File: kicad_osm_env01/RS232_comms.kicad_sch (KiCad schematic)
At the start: 17 parts

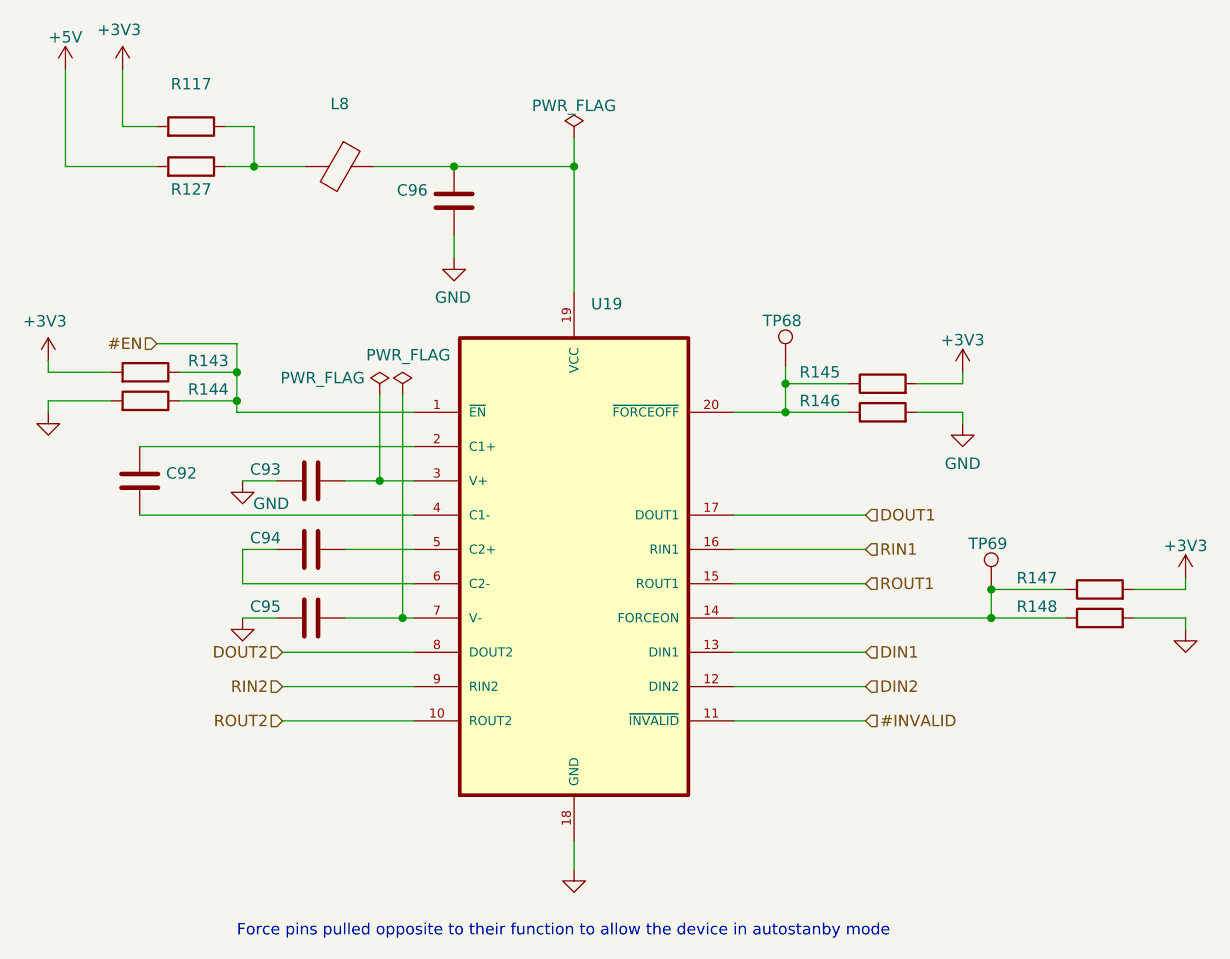
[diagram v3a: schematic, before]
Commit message: majority of signals routed on layout
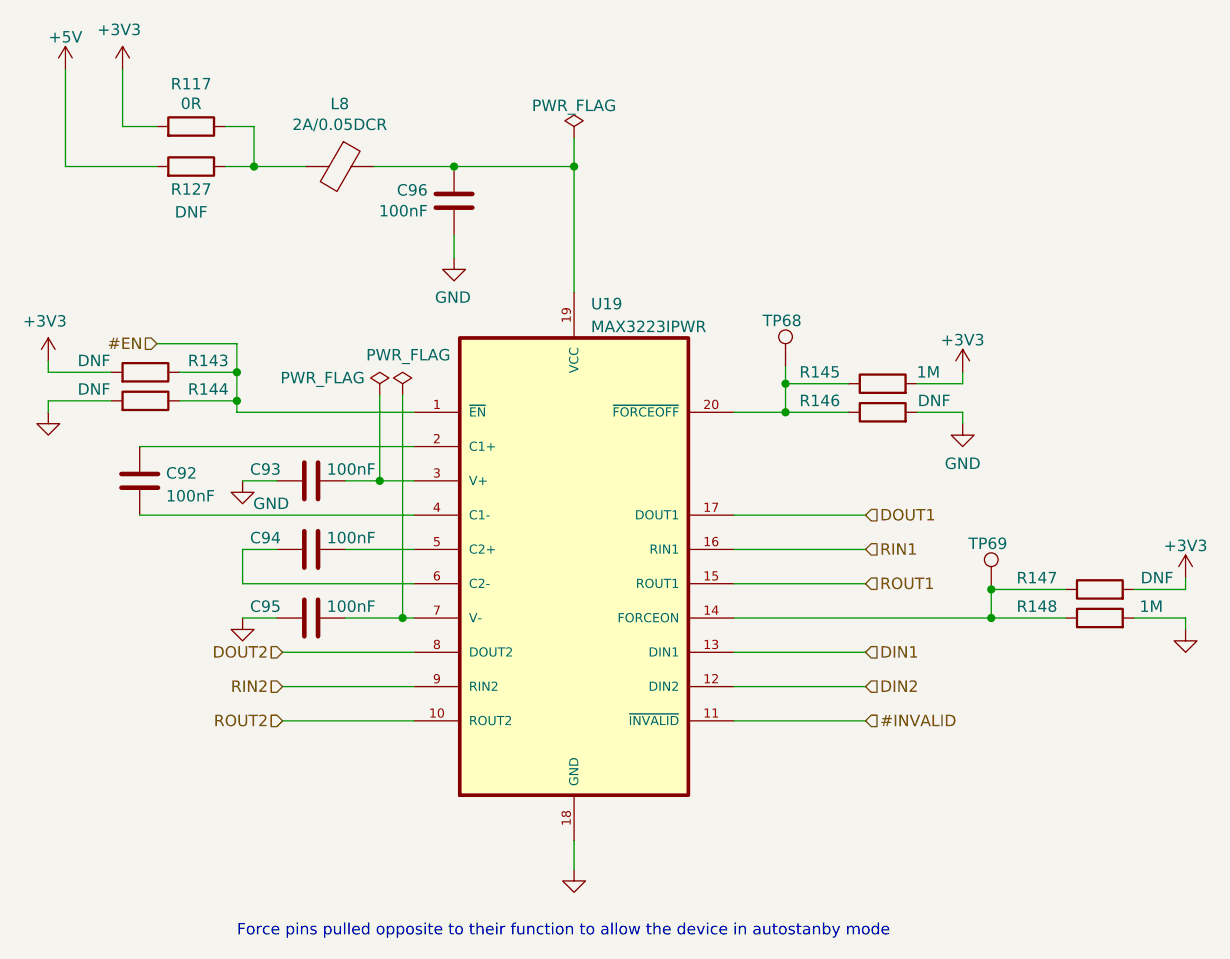
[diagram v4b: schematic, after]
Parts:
- C92, C93, C94, C95, C96: value (none) -> 100nF; footprint (none) -> Capacitor_SMD:C_0402_1005Metric
- L8: value (none) -> 2A/0.05DCR; footprint (none) -> Inductor_SMD:L_0402_1005Metric
- R117: value (none) -> 0R; footprint (none) -> Resistor_SMD:R_0603_1608Metric
- R127, R143, R144, R146, R147: value (none) -> DNF; footprint (none) -> Resistor_SMD:R_0603_1608Metric
- R145, R148: value (none) -> 1M; footprint (none) -> Resistor_SMD:R_0603_1608Metric
- TP68, TP69: value (none) -> Test_Point; footprint (none) -> TestPoint:TestPoint_THTPad_D1.0mm_Drill0.5mm
- U19: value (none) -> MAX3223IPWR; footprint (none) -> Package_SO:TSSOP-20_4.4x6.5mm_P0.65mm
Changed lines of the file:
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@@
     (in_bom yes) (on_board yes)
     (property "Reference" "L8" (id 0) (at 123.19 49.5554 90))
-    (property "Value" "" (id 1) (at 123.19 51.8668 90))
-    (property "Footprint" "" (id 2) (at 123.19 54.737 90)
+    (property "Value" "2A/0.05DCR" (id 1) (at 123.19 51.8668 90))
+    (property "Footprint" "Inductor_SMD:L_0402_1005Metric" (id 2) (at 123.19 54.737 90)
       (effects (font (size 1.27 1.27)) hide)
     )
@@
     (in_bom yes) (on_board yes)
     (property "Reference" "R117" (id 0) (at 106.68 47.3542 90))
-    (property "Value" "" (id 1) (at 106.68 49.53 90))
-    (property "Footprint" "" (id 2) (at 106.68 53.848 90)
+    (property "Value" "0R" (id 1) (at 106.68 49.53 90))
+    (property "Footprint" "Resistor_SMD:R_0603_1608Metric" (id 2) (at 106.68 53.848 90)
       (effects (font (size 1.27 1.27)) hide)
     )
@@
       (effects (font (size 1.27 1.27)) (justify left))
     )
-    (property "Value" "" (id 1) (at 132.969 61.468 0)
-      (effects (font (size 1.27 1.27)) (justify left))
-    )
-    (property "Footprint" "" (id 2) (at 134.9248 64.135 0)
+    (property "Value" "100nF" (id 1) (at 132.969 61.468 0)
+      (effects (font (size 1.27 1.27)) (justify left))
+    )
+    (property "Footprint" "Capacitor_SMD:C_0402_1005Metric" (id 2) (at 134.9248 64.135 0)
       (effects (font (size 1.27 1.27)) hide)
     )
@@
       (effects (font (size 1.27 1.27)) (justify left))
     )
-    (property "Value" "" (id 1) (at 151.1047 74.3259 0)
-      (effects (font (size 1.27 1.27)) (justify left))
-    )
-    (property "Footprint" "" (id 2) (at 149.225 100.965 0)
+    (property "Value" "MAX3223IPWR" (id 1) (at 151.1047 74.3259 0)
+      (effects (font (size 1.27 1.27)) (justify left))
+    )
+    (property "Footprint" "Package_SO:TSSOP-20_4.4x6.5mm_P0.65mm" (id 2) (at 149.225 100.965 0)
       (effects (font (size 1.27 1.27)) (justify left bottom) hide)
     )
@@
     (in_bom yes) (on_board yes)
     (property "Reference" "R144" (id 0) (at 108.585 81.28 90))
-    (property "Value" "" (id 1) (at 95.885 81.28 90))
-    (property "Footprint" "" (id 2) (at 101.6 84.328 90)
+    (property "Value" "DNF" (id 1) (at 95.885 81.28 90))
+    (property "Footprint" "Resistor_SMD:R_0603_1608Metric" (id 2) (at 101.6 84.328 90)
       (effects (font (size 1.27 1.27)) hide)
     )
@@
       (effects (font (size 1.27 1.27)) (justify left))
     )
-    (property "Value" "" (id 1) (at 103.886 93.1422 0)
-      (effects (font (size 1.27 1.27)) (justify left))
-    )
-    (property "Footprint" "" (id 2) (at 101.9302 95.25 0)
+    (property "Value" "100nF" (id 1) (at 103.886 93.1422 0)
+      (effects (font (size 1.27 1.27)) (justify left))
+    )
+    (property "Footprint" "Capacitor_SMD:C_0402_1005Metric" (id 2) (at 101.9302 95.25 0)
       (effects (font (size 1.27 1.27)) hide)
     )
@@
       (effects (font (size 1.27 1.27)) (justify left))
     )
-    (property "Value" "" (id 1) (at 174.117 77.1402 0)
+    (property "Value" "Test_Point" (id 1) (at 174.117 77.1402 0)
       (effects (font (size 1.27 1.27)) (justify left) hide)
     )
-    (property "Footprint" "" (id 2) (at 177.8 78.74 0)
+    (property "Footprint" "TestPoint:TestPoint_THTPad_D1.0mm_Drill0.5mm" (id 2) (at 177.8 78.74 0)
       (effects (font (size 1.27 1.27)) hide)
     )
@@
     (in_bom yes) (on_board yes)
     (property "Reference" "R127" (id 0) (at 106.68 59.055 90))
-    (property "Value" "" (id 1) (at 106.68 61.595 90))
-    (property "Footprint" "" (id 2) (at 106.68 58.293 90)
+    (property "Value" "DNF" (id 1) (at 106.68 61.595 90))
+    (property "Footprint" "Resistor_SMD:R_0603_1608Metric" (id 2) (at 106.68 58.293 90)
       (effects (font (size 1.27 1.27)) hide)
     )
@@
     (in_bom yes) (on_board yes)
     (property "Reference" "R145" (id 0) (at 176.53 79.375 90))
-    (property "Value" "" (id 1) (at 188.595 79.375 90))
-    (property "Footprint" "" (id 2) (at 183.515 82.423 90)
+    (property "Value" "1M" (id 1) (at 188.595 79.375 90))
+    (property "Footprint" "Resistor_SMD:R_0603_1608Metric" (id 2) (at 183.515 82.423 90)
       (effects (font (size 1.27 1.27)) hide)
     )
@@
     (in_bom yes) (on_board yes)
     (property "Reference" "R147" (id 0) (at 200.66 102.235 90))
-    (property "Value" "" (id 1) (at 213.995 102.235 90))
-    (property "Footprint" "" (id 2) (at 207.645 105.283 90)
+    (property "Value" "DNF" (id 1) (at 213.995 102.235 90))
+    (property "Footprint" "Resistor_SMD:R_0603_1608Metric" (id 2) (at 207.645 105.283 90)
       (effects (font (size 1.27 1.27)) hide)
     )
@@
     (in_bom yes) (on_board yes)
     (property "Reference" "C93" (id 0) (at 114.935 90.17 90))
-    (property "Value" "" (id 1) (at 124.46 90.17 90))
-    (property "Footprint" "" (id 2) (at 123.825 90.4748 0)
+    (property "Value" "100nF" (id 1) (at 124.46 90.17 90))
+    (property "Footprint" "Capacitor_SMD:C_0402_1005Metric" (id 2) (at 123.825 90.4748 0)
       (effects (font (size 1.27 1.27)) hide)
     )
@@
     (in_bom yes) (on_board yes)
     (property "Reference" "C94" (id 0) (at 114.935 97.79 90))
-    (property "Value" "" (id 1) (at 124.46 97.79 90))
-    (property "Footprint" "" (id 2) (at 123.825 98.0948 0)
+    (property "Value" "100nF" (id 1) (at 124.46 97.79 90))
+    (property "Footprint" "Capacitor_SMD:C_0402_1005Metric" (id 2) (at 123.825 98.0948 0)
       (effects (font (size 1.27 1.27)) hide)
     )
@@
     (in_bom yes) (on_board yes)
     (property "Reference" "C95" (id 0) (at 114.935 105.41 90))
-    (property "Value" "" (id 1) (at 124.46 105.41 90))
-    (property "Footprint" "" (id 2) (at 123.825 105.7148 0)
+    (property "Value" "100nF" (id 1) (at 124.46 105.41 90))
+    (property "Footprint" "Capacitor_SMD:C_0402_1005Metric" (id 2) (at 123.825 105.7148 0)
       (effects (font (size 1.27 1.27)) hide)
     )
@@
     (in_bom yes) (on_board yes)
     (property "Reference" "R148" (id 0) (at 200.66 105.41 90))
-    (property "Value" "" (id 1) (at 213.36 105.41 90))
-    (property "Footprint" "" (id 2) (at 207.645 108.458 90)
+    (property "Value" "1M" (id 1) (at 213.36 105.41 90))
+    (property "Footprint" "Resistor_SMD:R_0603_1608Metric" (id 2) (at 207.645 108.458 90)
       (effects (font (size 1.27 1.27)) hide)
     )
@@
     (in_bom yes) (on_board yes)
     (property "Reference" "R143" (id 0) (at 108.585 78.105 90))
-    (property "Value" "" (id 1) (at 95.885 78.105 90))
-    (property "Footprint" "" (id 2) (at 101.6 81.153 90)
+    (property "Value" "DNF" (id 1) (at 95.885 78.105 90))
+    (property "Footprint" "Resistor_SMD:R_0603_1608Metric" (id 2) (at 101.6 81.153 90)
       (effects (font (size 1.27 1.27)) hide)
     )
@@
     (in_bom yes) (on_board yes)
     (property "Reference" "R146" (id 0) (at 176.53 82.55 90))
-    (property "Value" "" (id 1) (at 189.23 82.55 90))
-    (property "Footprint" "" (id 2) (at 183.515 85.598 90)
+    (property "Value" "DNF" (id 1) (at 189.23 82.55 90))
+    (property "Footprint" "Resistor_SMD:R_0603_1608Metric" (id 2) (at 183.515 85.598 90)
       (effects (font (size 1.27 1.27)) hide)
     )
@@
       (effects (font (size 1.27 1.27)) (justify left))
     )
-    (property "Value" "" (id 1) (at 196.977 101.9052 0)
+    (property "Value" "Test_Point" (id 1) (at 196.977 101.9052 0)
       (effects (font (size 1.27 1.27)) (justify left) hide)
     )
-    (property "Footprint" "" (id 2) (at 200.66 103.505 0)
-      (effects (font (size 1.27 1.27)) hide)
-    )
+    (property "Footprint" "TestPoint:TestPoint_THTPad_D1.0mm_Drill0.5mm" (id 2) (at 200.66 103.505 0)
+      (effects (font (size 1.27 1.27)) hide)
+    )
